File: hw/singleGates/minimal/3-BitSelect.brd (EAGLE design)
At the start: 36 parts, among them Q1 BC817, Q10 BC817, Q11 BC817, Q12 BC817, Q13 BC817, Q14 BC817, Q15 BC817, Q16 BC817, Q17 BC817, Q2 BC817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

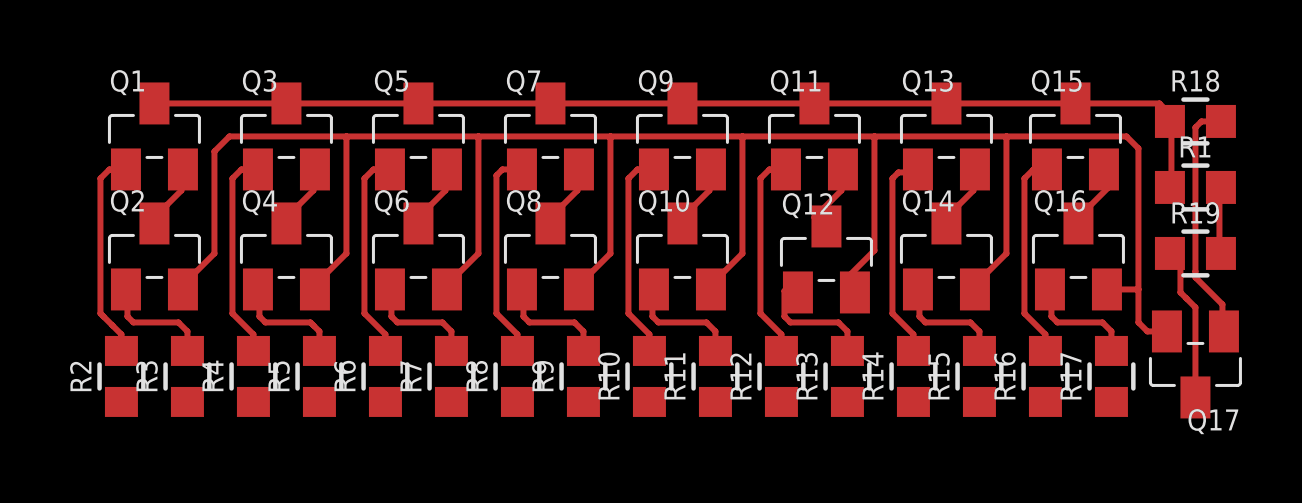
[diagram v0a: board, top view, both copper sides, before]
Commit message: Add led output and prepare first alu slice
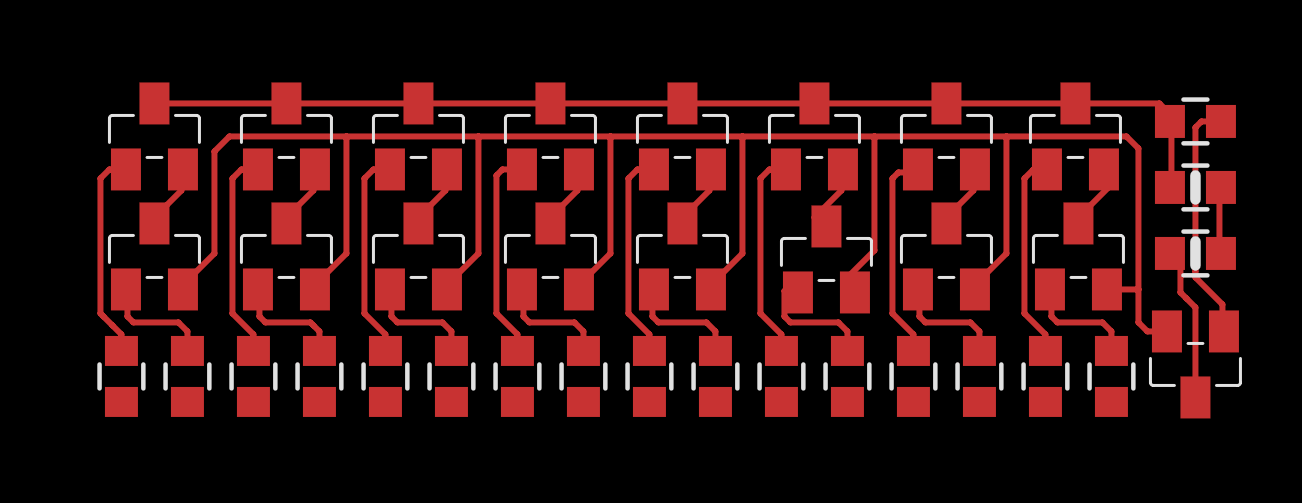
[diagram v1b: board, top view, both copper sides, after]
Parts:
- R1, R19: device p.peter-gator:R0603 -> p.peter-rcl:R0603-MARK
